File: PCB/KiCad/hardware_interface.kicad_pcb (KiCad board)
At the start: 6 copper layers, 86 x 86 mm, 252 parts, among them J1 Reset Header, J10 I2C1, J11 I2C1, J12 TIM1, J13 TIM2, J14 I2C2, J15 I2C2, J16 I2C2, J17 I2C2, J18 3.3V Out, J19 5V Out, J2 SWD Flash, J20 UART1, J21 UART2, J22 UART3, J23 Servo 1, J24 Servo 2, J25 GPIO, J26 Analog 1, J27 Analog 2, J28 USB1, J29 USB2, J3 XT30, J30 LED1, J31 LED2, J4 CAN1, J5 CAN1, J6 SPI1, J7 SPI1, J8 I2C1, J9 I2C1, SW1 Reset, SW2 User Button, U1 STM32F429ZIT6TR, U10 USBLC6-2SC6, U11 TCAN1057AVDRQ1, U12 USBLC6-2SC6, U2 TPS2117DRLR, U3 MIC2039AYM6-TR, U4 OPA2834IDGKR, U5 OPA2834IDGKR, U6 SN74S1051DR, U7 SN74S1051DR, U8 SN74S1051DR, U9 SN74S1051DR, Y1 IQXO-791 8.00MHz

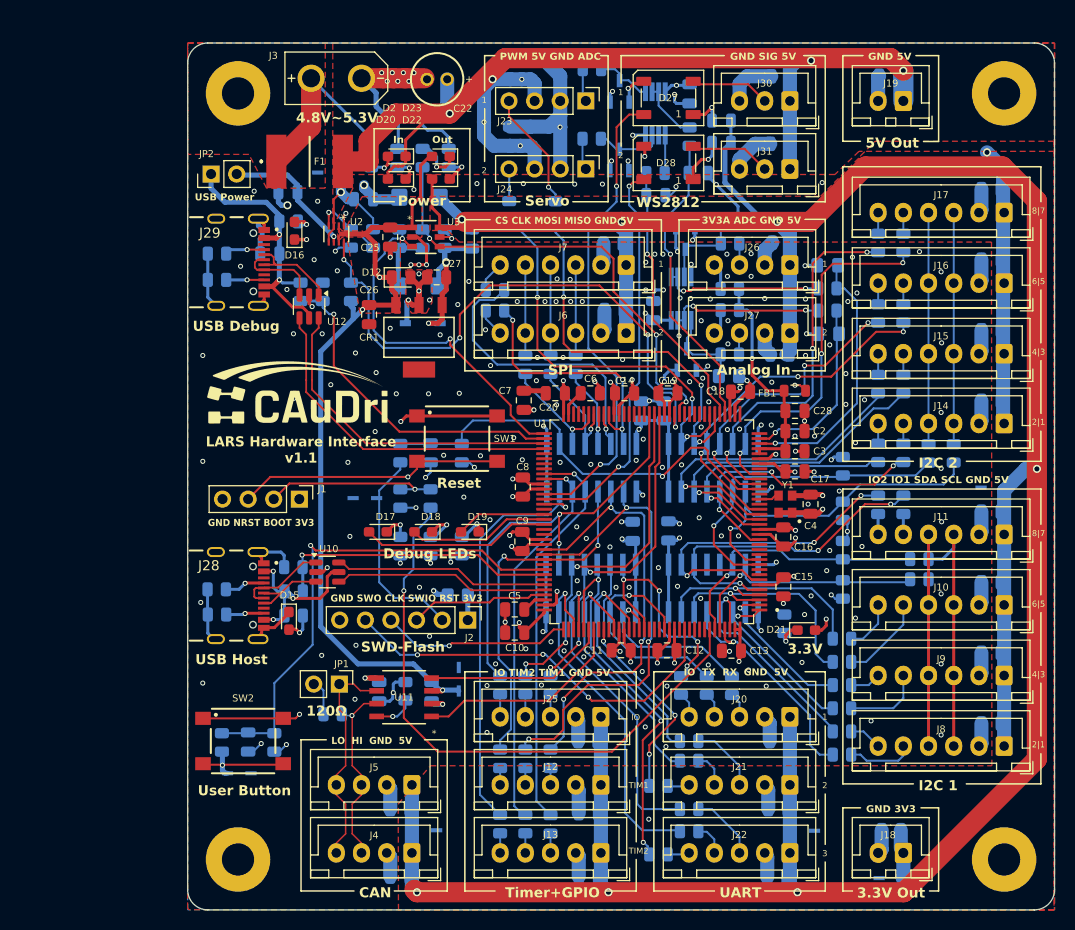
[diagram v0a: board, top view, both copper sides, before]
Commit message: PCB: update drawing sheet
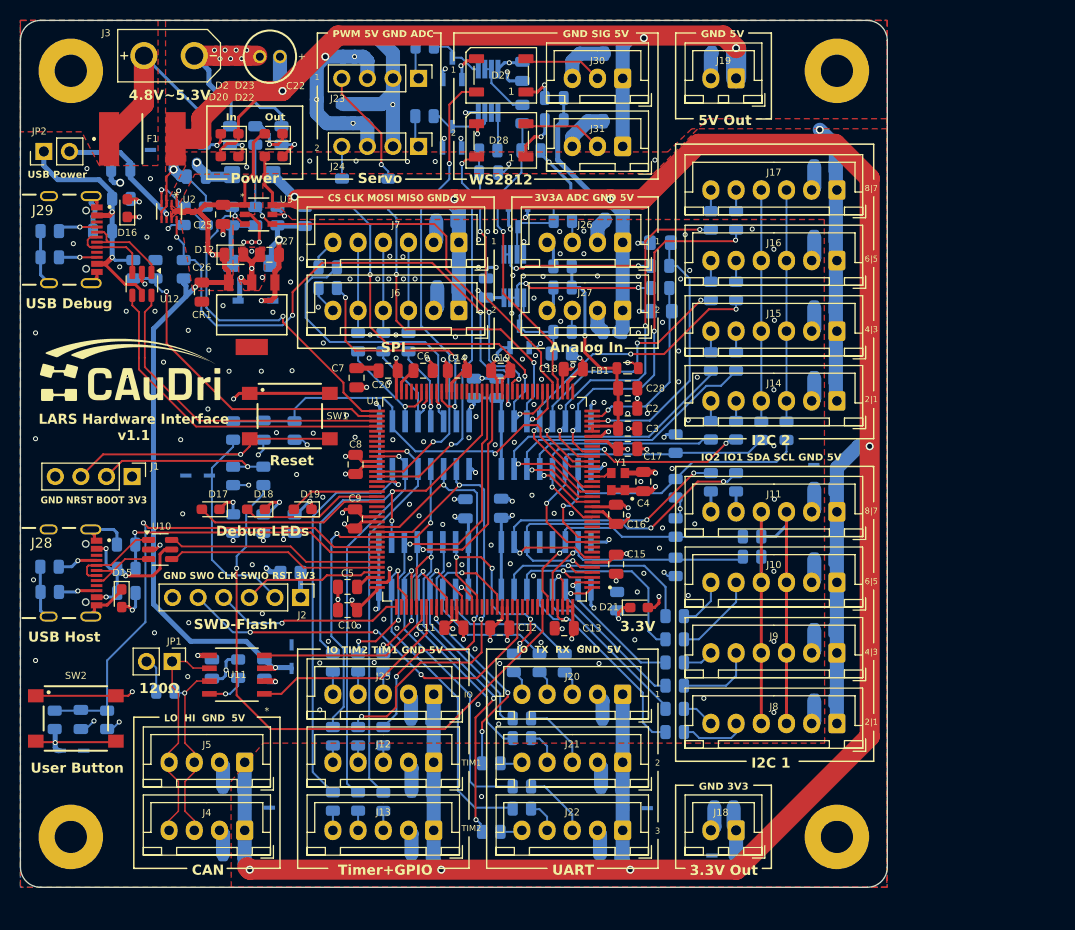
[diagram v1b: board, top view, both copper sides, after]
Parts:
- moved C19 16.7 mm to (125.2, 87.7)
- moved R19 16.7 mm to (117.6, 62.4)
- moved R33 16.7 mm to (124.3, 133.4)
- moved C61 16.7 mm to (121.7, 101.4)
- moved CR5 16.7 mm to (120.4, 64.5)
- moved R32 16.7 mm to (124.3, 126.6)
- moved U5 16.7 mm to (124.0, 59.9)
- moved C11 16.7 mm to (120.6, 113.2)
- moved C13 16.7 mm to (131.5, 113.2)
- moved C14 16.7 mm to (120.9, 87.7)
- moved C16 16.7 mm to (136.7, 101.9)
- moved C17 16.7 mm to (137.8, 95.4)
- moved C2 16.7 mm to (137.8, 91.4)
- moved C20 16.7 mm to (114.0, 87.7)
- moved C22 16.7 mm to (102.3, 56.5)
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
